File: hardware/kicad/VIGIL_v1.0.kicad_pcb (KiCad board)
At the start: 2 copper layers, 185 x 35 mm, 20 parts, among them J1 USB-C [HAND SOLDER], J2 BAT [HAND SOLDER], U1 nRF52840, U2 LIS3DHTR, U3 TMP117, U4 ICS-43434 [HAND SOLDER], U5 AD8606, U6 TPS62840 [HAND SOLDER], U7 BQ24072, Y1 32.768kHz [HAND SOLDER]

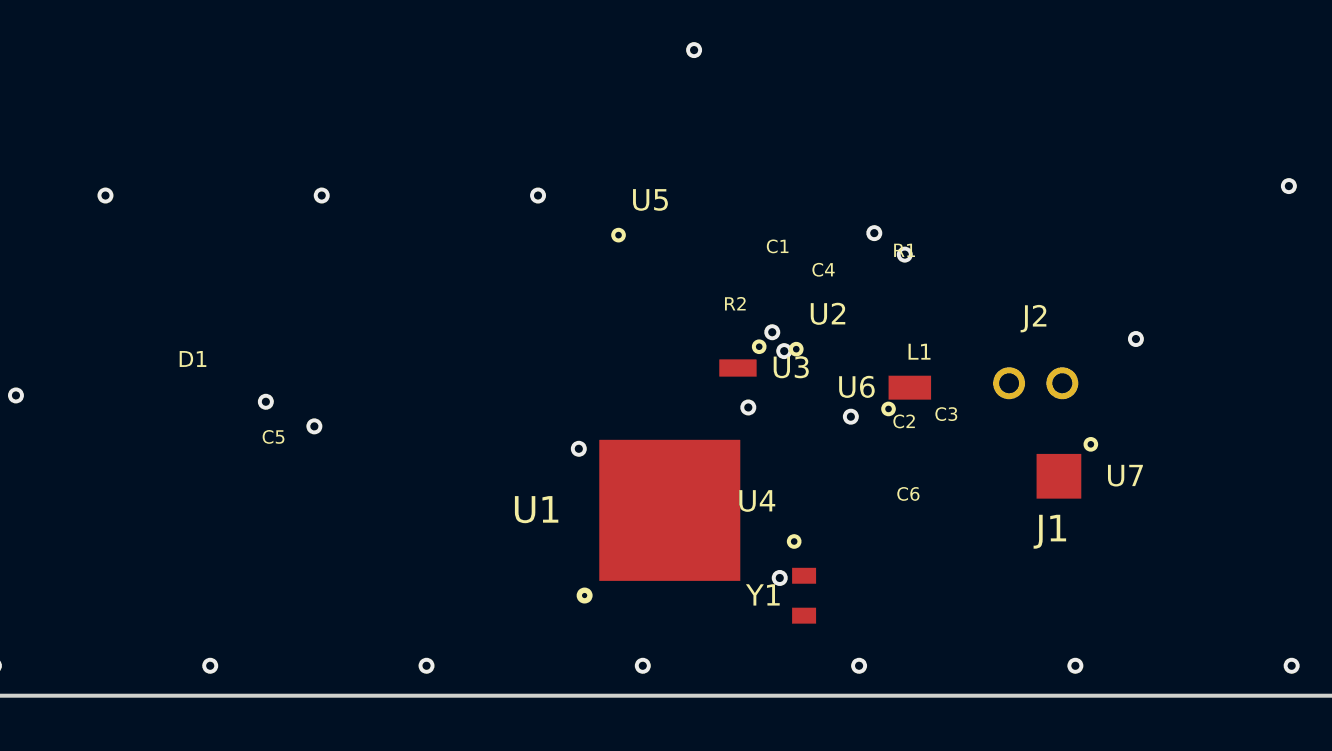
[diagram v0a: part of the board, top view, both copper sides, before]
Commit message: Fix KiCad PCB file with proper syntax and UUIDs
- Regenerate .kicad_pcb using Python for correct KiCad 8 format
- Add UUIDs to all elements (required by KiCad 8)
- Add proper net definitions, pad definitions, and setup block
- Add SVG layout viewer as fallback
- Include build script for reproducibility

Co-Authored-By: Claude Opus 4.6 (1M context) <noreply@anthropic.com>
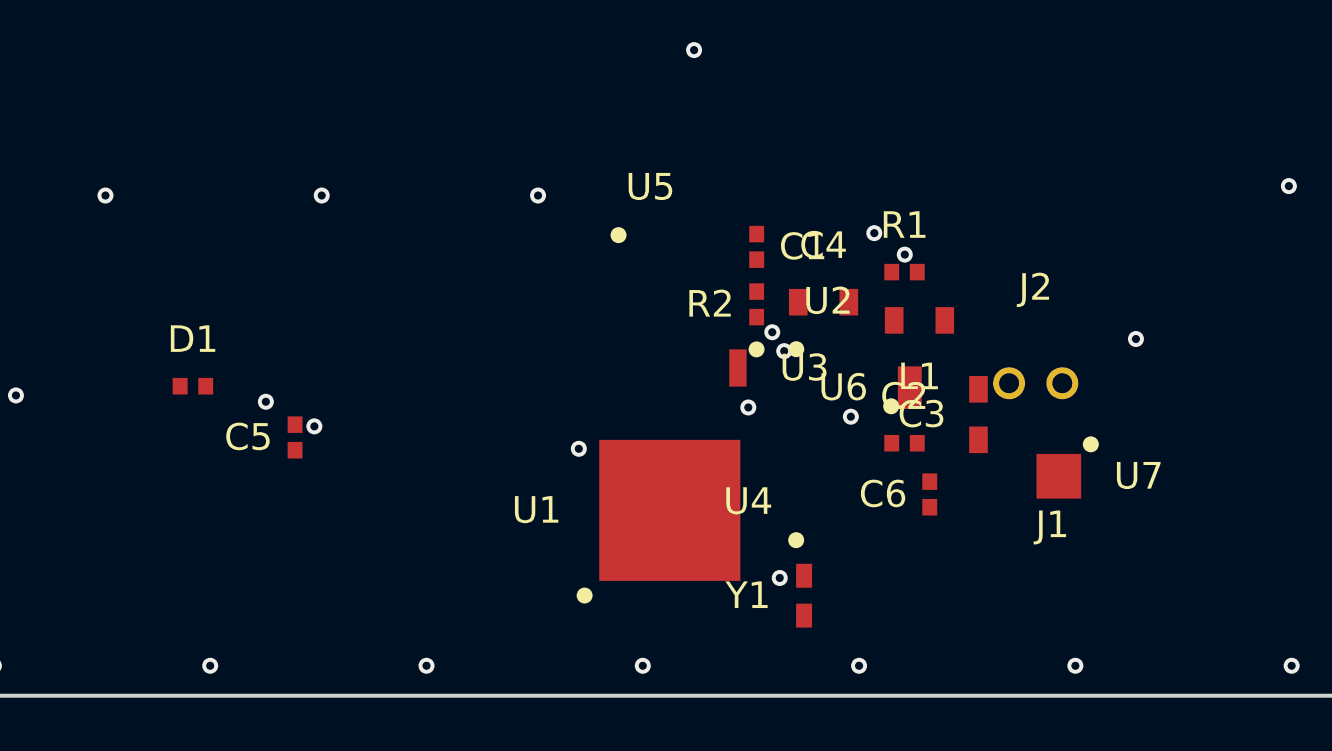
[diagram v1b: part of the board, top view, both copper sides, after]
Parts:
- C1, C2, C5, C6: footprint Capacitor_SMD:C_0402_1005Metric -> C_0402
- C3, C4: footprint Capacitor_SMD:C_0805_2012Metric -> C_0805
- D1: footprint LED_SMD:LED_0402_1005Metric -> LED_0402
- J1: value USB-C [HAND SOLDER] -> USB_C [HAND SOLDER]; footprint Connector_USB:USB_C_Receptacle_GCT_USB4105-GF-A -> USB_C_GCT_USB4105
- J2: value BAT [HAND SOLDER] -> BAT_JST_PH [HAND SOLDER]; footprint Connector_JST:JST_PH_B2B-PH-K_1x02_P2.00mm_Vertical -> JST_PH_B2B-PH-K
- L1: footprint Inductor_SMD:L_0805_2012Metric -> L_0805
- R1, R2: footprint Resistor_SMD:R_0402_1005Metric -> R_0402
- U1: value nRF52840 -> nRF52840-QIAA; footprint Package_DFN_QFN:QFN-73-1EP_7x7mm_P0.4mm_EP5.3x5.3mm -> QFN-73-1EP_7x7mm
- U2: footprint Package_LGA:LGA-16_3x3mm_P0.5mm -> LGA-16_3x3mm
- U3: value TMP117 -> TMP117AIDRVR; footprint Package_SON:WSON-6-1EP_2x2mm_P0.65mm_EP0.65x1.4mm -> WSON-6_2x2mm
- U4: footprint Package_LGA:LGA-6_3.5x2.65mm_P1.27mm -> LGA-6_3.5x2.65mm
- U5: value AD8606 -> AD8606ARMZ; footprint Package_SO:MSOP-8_3x3mm_P0.65mm -> MSOP-8_3x3mm
- U6: value TPS62840 [HAND SOLDER] -> TPS62840DLCR [HAND SOLDER]; footprint Package_SON:WSON-8-1EP_2x2mm_P0.5mm_EP0.9x1.6mm -> WSON-8_2x2mm
- U7: value BQ24072 -> BQ24072RGTR; footprint Package_DFN_QFN:QFN-16-1EP_3x3mm_P0.5mm_EP1.68x1.68mm -> QFN-16_3x3mm
- Y1: footprint Crystal:Crystal_SMD_2012-2Pin_2.0x1.2mm -> Crystal_SMD_2012
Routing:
- net GND: vias 0 -> 106
- net (no net): vias 106 -> 0
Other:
- board text added: "FLEX TAIL"
- board text removed: "FLEX TAIL (to temple)"
